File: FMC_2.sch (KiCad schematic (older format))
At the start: 14 parts, among them P2 SAMTEC_ASP-134486-01

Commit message: FMC HPC & LPC done, FPGA power delivery done, RGMII lines done,  MGT lines progress
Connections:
- net labels added: FMC2_DP0_C2M_N, FMC2_DP0_C2M_P, FMC2_DP0_M2C_N, FMC2_DP0_M2C_P
- wire segments 599 -> 603
- no-connect marks 5 -> 1
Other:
- moved on the sheet: C10, C9, P2A, P2B, P2E, P2F, P2I, P2J, R258, R259

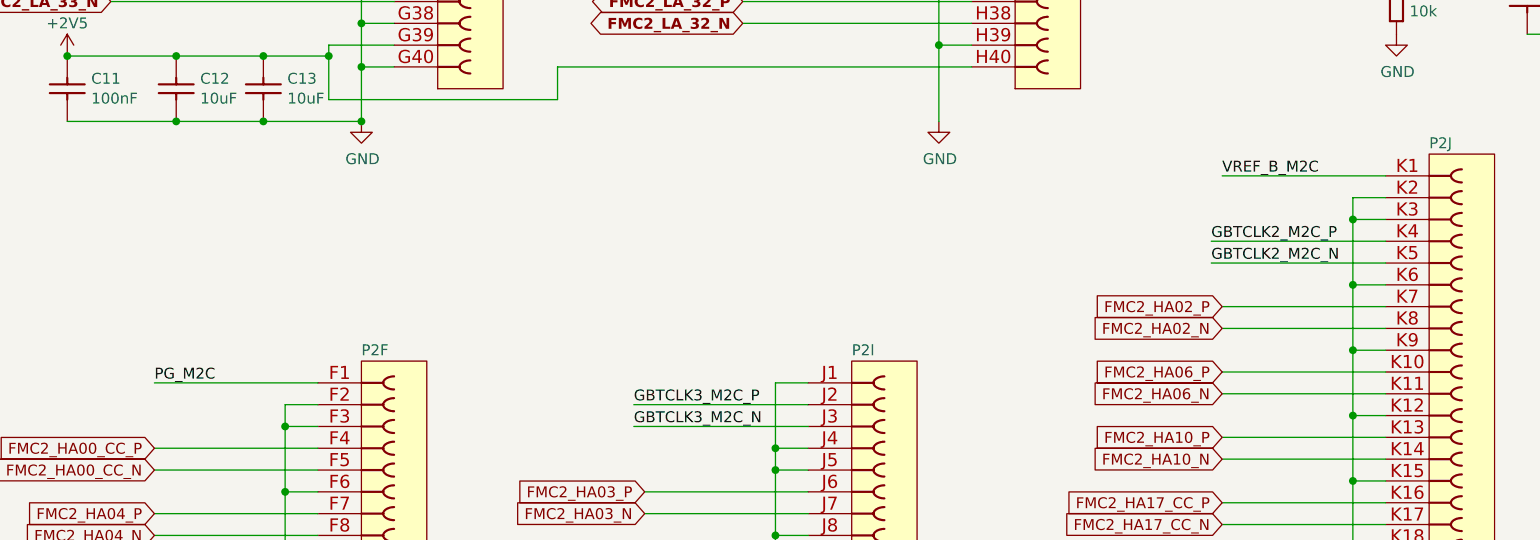
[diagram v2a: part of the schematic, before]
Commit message: FPGA power finished, significant progress on PCB
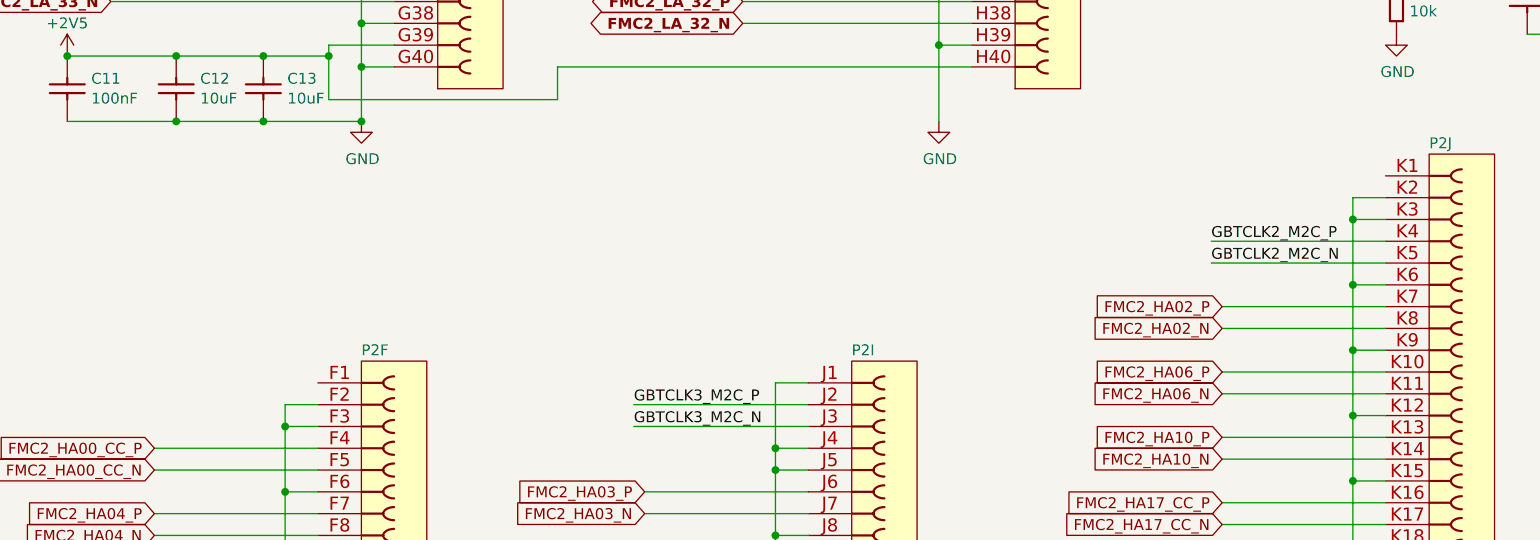
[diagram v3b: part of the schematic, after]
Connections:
- net labels removed: PG_M2C, VREF_B_M2C
- wire segments 603 -> 601
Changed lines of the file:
@@
 	13700 950  14600 950
 $Comp
-L AMC_FMC_Carrier-PcbDoc-rescue:+12V_FMC2-powerMG-AMC_FMC_Carrier-PcbDoc-rescue #PWR01
+L AMC_FMC_Carrier-PcbDoc-rescue:+12V_FMC2-powerMG-AMC_FMC_Carrier-PcbDoc-rescue-AMC_FMC_Carrier-PcbDoc-rescue-AMC_FMC_Carrier-PcbDoc-rescue #PWR01
 U 1 1 5BFC3656
 P 2200 4650
@@
 	6100 6900 6100 7000
 Wire Wire Line
-	7500 6600 8250 6600
-Wire Wire Line
 	7500 6900 8250 6900
 Wire Wire Line
@@
 Wire Wire Line
 	12400 9550 13150 9550
-Wire Wire Line
-	12400 5650 13150 5650
 Text Label 12350 5950 0    50   ~ 0
 GBTCLK2_M2C_P
@@
 Text GLabel 12400 9350 0    50   Input ~ 0
 FMC2_HB17_CC_N
-Text Label 12400 5650 0    50   ~ 0
-VREF_B_M2C
-Text Label 7500 6600 0    50   ~ 0
-PG_M2C
 $Comp
 L power:+2V5 #PWR0678

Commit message: new board outline, rearranging banks connections, SODIMM memory
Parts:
- removed F1: FUS0603_BOURNS-SF-0603F050-2, FUSC1608X55N, symbol Fuses:FUS0603_BOURNS-SF-0603F050-2
- added R78: R0603_10R_1%_0.1W_200PPM, Resistors SMD:RESC1608X55N, symbol Resistors_SMD:R0603_10R_1%_0.1W_200PPM
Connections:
- net labels added: FMC2_GBTCLK1_M2C_N, FMC2_GBTCLK1_M2C_P, PG_M2C, VREF_B_M2C
- net labels removed: GBTCLK1_M2C_N, GBTCLK1_M2C_P
- wire segments 601 -> 605
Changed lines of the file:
@@
 EESchema Schematic File Version 4
-LIBS:AMC_FMC_Carrier-PcbDoc-cache
 EELAYER 30 0
 EELAYER END
@@
 Text Label 13750 1600 0    50   ~ 10
 I2C_FMC2_SDA
-Text Label 13700 3450 0    50   ~ 10
+Text Label 13700 2800 0    50   ~ 10
 FMC2_GBTCLK0_M2C_P
-Text Label 13700 3550 0    50   ~ 10
+Text Label 13700 2900 0    50   ~ 10
 FMC2_GBTCLK0_M2C_N
 Text Label 13750 2250 0    50   ~ 10
@@
 Wire Wire Line
 	13700 4050 14600 4050
-Text HLabel 14600 3450 2    50   Output ~ 10
+Text HLabel 14600 2800 2    50   Output ~ 10
 FMC2_GBTCLK0_M2C_P
-Text HLabel 14600 3550 2    50   Output ~ 10
+Text HLabel 14600 2900 2    50   Output ~ 10
 FMC2_GBTCLK0_M2C_N
 Text HLabel 14600 3700 2    50   Output ~ 10
@@
 FMC2_CLK0_M2C_N
 Wire Wire Line
-	13700 3450 14600 3450
+	13700 2800 14600 2800
 Wire Wire Line
-	13700 3550 14600 3550
+	13700 2900 14600 2900
 Text HLabel 14600 1150 2    50   Output ~ 10
 FMC2_PRSNT_M2C_L
@@
 	13700 950  14600 950
 $Comp
-L AMC_FMC_Carrier-PcbDoc-rescue:+12V_FMC2-powerMG-AMC_FMC_Carrier-PcbDoc-rescue-AMC_FMC_Carrier-PcbDoc-rescue-AMC_FMC_Carrier-PcbDoc-rescue #PWR01
+L AMC_FMC_Carrier-PcbDoc-rescue:+12V_FMC2-powerMG-AMC_FMC_Carrier-PcbDoc-rescue-AMC_FMC_Carrier-PcbDoc-rescue #PWR01
 U 1 1 5BFC3656
 P 2200 4650
@@
 	1    0    0    -1
 $EndComp
-Wire Wire Line
-	15000 4700 15150 4700
 $Comp
 L power:+2V5 #PWR?
@@
 Connection ~ 2200 4650
 Connection ~ 2200 4950
-$Comp
-L Fuses:FUS0603_BOURNS-SF-0603F050-2 F?
-U 1 1 5DA6452C
-P 14700 4700
-AR Path="/5BD31F9A/5DA6452C" Ref="F?"  Part="1"
-AR Path="/5BD31F9F/5DA6452C" Ref="F1"  Part="1"
-F 0 "F1" H 14850 4897 50  0000 C CNN
-F 1 "FUS0603_BOURNS-SF-0603F050-2" H 14700 4480 60  0001 L CNN
-F 2 "FUSC1608X55N" H 14700 3670 60  0001 L CNN
-F 3 "\\\\cern.ch\\dfs\\Applications\\Altium\\Datasheets\\FUSE_BOURNS_SF-0603F.pdf" H 14700 4300 60  0001 L CNN
-F 4 "500mA-50V" H 14850 4806 50  0000 C CNN "~"
-F 5 "FUS0603_BOURNS-SF-0603F050-2" H 14700 4210 60  0001 L CNN "Part Number"
-F 6 "Fuse" H 14700 4120 60  0001 L CNN "Library Ref"
-F 7 "SchLib\\Fuses.SchLib" H 14700 4030 60  0001 L CNN "Library Path"
-F 8 "=Value" H 14700 3940 60  0001 L CNN "Comment"
-F 9 "Standard" H 14700 3850 60  0001 L CNN "Component Kind"
-F 10 "Standard" H 14700 3760 60  0001 L CNN "Component Type"
-F 11 "2" H 14700 3580 60  0001 L CNN "Pin Count"
-F 12 "~~" H 14700 3490 60  0001 L CNN "Case"
-F 13 "PcbLib\\Fuses.PcbLib" H 14700 3400 60  0001 L CNN "Footprint Path"
-F 14 "FUSC1608X55N" H 14700 3310 60  0001 L CNN "Footprint Ref"
-F 15 "Chip Fuse, 2-Leads, Body 1.6mm x 0.8mm, IPC Medium Density" H 14700 3220 60  0001 L CNN "PackageDescription"
-F 16 "Fuse" H 14700 3130 60  0001 L CNN "Family"
-F 17 "Yes" H 14700 3040 60  0001 L CNN "Mounted"
-F 18 "No" H 14700 2950 60  0001 L CNN "Socket"
-F 19 "Yes" H 14700 2860 60  0001 L CNN "SMD"
-F 20 "No" H 14700 2770 60  0001 L CNN "PressFit"
-F 21 "No" H 14700 2680 60  0001 L CNN "Sense"
-F 22 "~~" H 14700 2590 60  0001 L CNN "Sense Comment"
-F 23 "~~" H 14700 2500 60  0001 L CNN "Status"
-F 24 "~~" H 14700 2410 60  0001 L CNN "Status Comment"
-F 25 "~~" H 14700 2320 60  0001 L CNN "SCEM"
-F 26 "500mA-50V" H 14700 2230 60  0001 L CNN "Val"
-F 27 "Thin Film Chip Fuse" H 14700 2140 60  0001 L CNN "Part Description"
-F 28 "BOURNS" H 14700 2050 60  0001 L CNN "Manufacturer"
-F 29 "SF-0603F050-2" H 14700 1960 60  0001 L CNN "Manufacturer Part Number"
-F 30 "0.55mm" H 14700 1870 60  0001 L CNN "ComponentHeight"
-F 31 "~~" H 14700 1780 60  0001 L CNN "Manufacturer1 Example"
-F 32 "~~" H 14700 1690 60  0001 L CNN "Manufacturer1 Part Number"
-F 33 "~~" H 14700 1600 60  0001 L CNN "Manufacturer1 ComponentHeight"
-F 34 "\\\\cern.ch\\dfs\\Applications\\Altium\\Datasheets\\FUSE_BOURNS_SF-0603F.pdf" H 14700 1510 60  0001 L CNN "HelpURL"
-F 35 "~~" H 14700 1420 60  0001 L CNN "ComponentLink1URL"
-F 36 "~~" H 14700 1330 60  0001 L CNN "ComponentLink1Description"
-F 37 "~~" H 14700 1240 60  0001 L CNN "ComponentLink2URL"
-F 38 "~~" H 14700 1150 60  0001 L CNN "ComponentLink2Description"
-F 39 "CERN DEM JLC" H 14700 1060 60  0001 L CNN "Author"
-F 40 "02/01/17 00:00:00" H 14700 970 60  0001 L CNN "CreateDate"
-F 41 "02/01/17 00:00:00" H 14700 880 60  0001 L CNN "LatestRevisionDate"
-F 42 "Fuses" H 14700 790 60  0001 L CNN "Library Name"
-F 43 "This work is licensed under the Creative Commons CC-BY-SA 4.0 License. To the extent that circuit schematics that use Licensed Material can be considered to be ‘Adapted Material’, then the copyright holder waives article 3.b of the license with respect to these schematics." H 14700 700 60  0001 L CNN "License"
-	1    14700 4700
-	1    0    0    -1
-$EndComp
 Text GLabel 10200 1850 0    50   BiDi ~ 10
 FMC2_LA_2_P
@@
 Wire Wire Line
 	3900 8000 3900 8300
-Text Label 3250 8500 0    50   ~ 0
-GBTCLK1_M2C_P
-Text Label 3250 8600 0    50   ~ 0
-GBTCLK1_M2C_N
-Wire Wire Line
-	3250 8500 4050 8500
-Wire Wire Line
-	3250 8600 4050 8600
 Wire Wire Line
 	3900 10300 4050 10300
@@
 	6100 6900 6100 7000
 Wire Wire Line
+	7500 6600 8250 6600
+Wire Wire Line
 	7500 6900 8250 6900
 Wire Wire Line
@@
 Wire Wire Line
 	12400 9550 13150 9550
+Wire Wire Line
+	12400 5650 13150 5650
 Text Label 12350 5950 0    50   ~ 0
 GBTCLK2_M2C_P
@@
 Text GLabel 12400 9350 0    50   Input ~ 0
 FMC2_HB17_CC_N
+Text Label 12400 5650 0    50   ~ 0
+VREF_B_M2C
+Text Label 7500 6600 0    50   ~ 0
+PG_M2C
 $Comp
 L power:+2V5 #PWR0678
@@
 Wire Wire Line
 	2450 1850 3550 1850
+$Comp
+L Resistors_SMD:R0603_10R_1%_0.1W_200PPM R78
+U 1 1 5EBACC52
+P 14700 4700
+F 0 "R78" H 14850 4897 50  0000 C CNN
+F 1 "R0603_10R_1%_0.1W_200PPM" H 14700 4505 50  0001 L CNN
+F 2 "Resistors SMD:RESC1608X55N" H 14700 4430 50  0001 L CNN
+F 3 " " H 14700 4355 50  0001 L CNN
+F 4 "10" H 14850 4806 50  0000 C CNN "Val"
+F 5 "R0603_10R_1%_0.1W_200PPM" H 14700 4280 50  0001 L CNN "Part Number"
+F 6 "Resistor - 1%" H 14700 4205 50  0001 L CNN "Library Ref"
+F 7 "SchLib\\Resistors.SchLib" H 14700 4130 50  0001 L CNN "Library Path"
+F 8 "10" H 14700 4055 50  0001 L CNN "Comment"
+F 9 "Standard" H 14700 3980 50  0001 L CNN "Component Kind"
+F 10 "Standard" H 14700 3905 50  0001 L CNN "Component Type"
+F 11 " " H 14700 3830 50  0001 L CNN "PackageDescription"
+F 12 "2" H 14700 3755 50  0001 L CNN "Pin Count"
+F 13 "PcbLib\\Resistors SMD.PcbLib" H 14700 3680 50  0001 L CNN "Footprint Path"
+F 14 "RESC1608X55N" H 14700 3605 50  0001 L CNN "Footprint Ref"
+F 15 "Preferred" H 14700 3530 50  0001 L CNN "Status"
+F 16 "0.1W" H 14700 3455 50  0001 L CNN "Power"
+F 17 "±200ppm/°C" H 14700 3380 50  0001 L CNN "TC"
+F 18 " " H 14700 3305 50  0001 L CNN "Voltage"
+F 19 "±1%" H 14700 3230 50  0001 L CNN "Tolerance"
+F 20 "General Purpose Thick Film Chip Resistor" H 14700 3155 50  0001 L CNN "Part Description"
+F 21 "GENERIC" H 14700 3080 50  0001 L CNN "Manufacturer"
+F 22 "R0603_10R_1%_0.1W_200PPM" H 14700 3005 50  0001 L CNN "Manufacturer Part Number"
+F 23 "0603" H 14700 2930 50  0001 L CNN "Case"
+F 24 "No" H 14700 2855 50  0001 L CNN "PressFit"
+F 25 "Yes" H 14700 2780 50  0001 L CNN "Mounted"
+F 26 " " H 14700 2705 50  0001 L CNN "Sense Comment"
+F 27 "No" H 14700 2630 50  0001 L CNN "Sense"
+F 28 " " H 14700 2555 50  0001 L CNN "Status Comment"
+F 29 "No" H 14700 2480 50  0001 L CNN "Socket"
+F 30 "Yes" H 14700 2405 50  0001 L CNN "SMD"
+F 31 " " H 14700 2330 50  0001 L CNN "ComponentHeight"
+F 32 "NIC COMPONENT" H 14700 2255 50  0001 L CNN "Manufacturer1 Example"
+F 33 "NRC06F10R0TRF" H 14700 2180 50  0001 L CNN "Manufacturer1 Part Number"
+F 34 "0.55mm" H 14700 2105 50  0001 L CNN "Manufacturer1 ComponentHeight"
+F 35 "CERN DEM JLC" H 14700 2030 50  0001 L CNN "Author"
+F 36 "12/03/07 00:00:00" H 14700 1955 50  0001 L CNN "CreateDate"
+F 37 "06/24/09 00:00:00" H 14700 1880 50  0001 L CNN "LatestRevisionDate"
+F 38 "Resistors SMD" H 14700 1805 50  0001 L CNN "Database Table Name"
+F 39 "Resistors.DbLib" H 14700 1730 50  0001 L CNN "Library Name"
+F 40 "Resistors SMD" H 14700 1655 50  0001 L CNN "Footprint Library"
+F 41 "This work is licensed under the Creative Commons CC-BY-SA 4.0 License. To the extent that circuit schematics that use Licensed Material can be considered to be ‘Adapted Material’, then the copyright holder waives article 3.b of the license with respect to these schematics." H 14700 1580 50  0001 L CNN "License"
+	1    14700 4700
+	1    0    0    -1
+$EndComp
+Wire Wire Line
+	15000 4700 15150 4700
+Text Label 13700 3050 0    50   ~ 10
+FMC2_GBTCLK1_M2C_P
+Text Label 13700 3150 0    50   ~ 10
+FMC2_GBTCLK1_M2C_N
+Text HLabel 14600 3050 2    50   Output ~ 10
+FMC2_GBTCLK1_M2C_P
+Text HLabel 14600 3150 2    50   Output ~ 10
+FMC2_GBTCLK1_M2C_N
+Wire Wire Line
+	13700 3050 14600 3050
+Wire Wire Line
+	13700 3150 14600 3150
+Text Label 2950 8500 0    50   ~ 10
+FMC2_GBTCLK1_M2C_P
+Text Label 2950 8600 0    50   ~ 10
+FMC2_GBTCLK1_M2C_N
+Wire Wire Line
+	2950 8500 4050 8500
+Wire Wire Line
+	2950 8600 4050 8600
 $EndSCHEMATC

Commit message: routing done
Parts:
- removed R78: R0603_10R_1%_0.1W_200PPM, Resistors SMD:RESC1608X55N, symbol Resistors_SMD:R0603_10R_1%_0.1W_200PPM
- added R11, R12: R0402_240R_1%_0.0625W_100PPM, Resistors SMD:RESC1005X40N, symbol Resistors_SMD:R0402_240R_1%_0.0625W_100PPM
- added U55: MIC2090-1YM5TR, ICs And Semiconductors SMD:SOT95P280X145-5N, symbol Analog_&_Interface:MIC2090-1YM5TR
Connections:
- net +3.3VP: now also R258.1, R259.1, U55.1 (VIN)
- net FMC2_3P3VAUX: now also R11.1, U55.5 (VOUT); no longer P2.C34 (c34), R259.1
- net FMC2_FUSE: now also R258.2, U55.4 (FAULT/); no longer R258.1, R259.2
- net GND: now also R12.1, U55.2 (GND); no longer P2.D35 (d35), R258.2
- new net: R259.2, U55.3 (EN)
- new net: P2.C34 (c34), R11.2
- new net: P2.D35 (d35), R12.2
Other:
- moved on the sheet: C10, C5, C6, C9, R258, R259

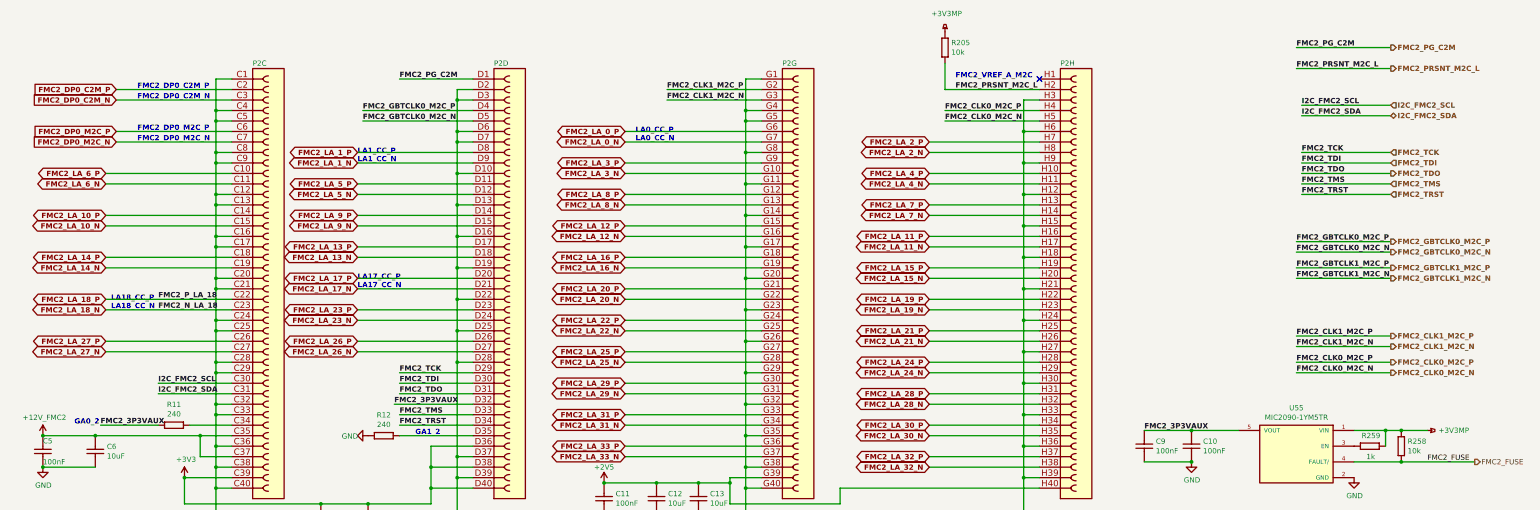
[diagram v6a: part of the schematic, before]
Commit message: DDR lenght mached, 2 additional LEDs added, I2C pullups voltage changed and other minor changes
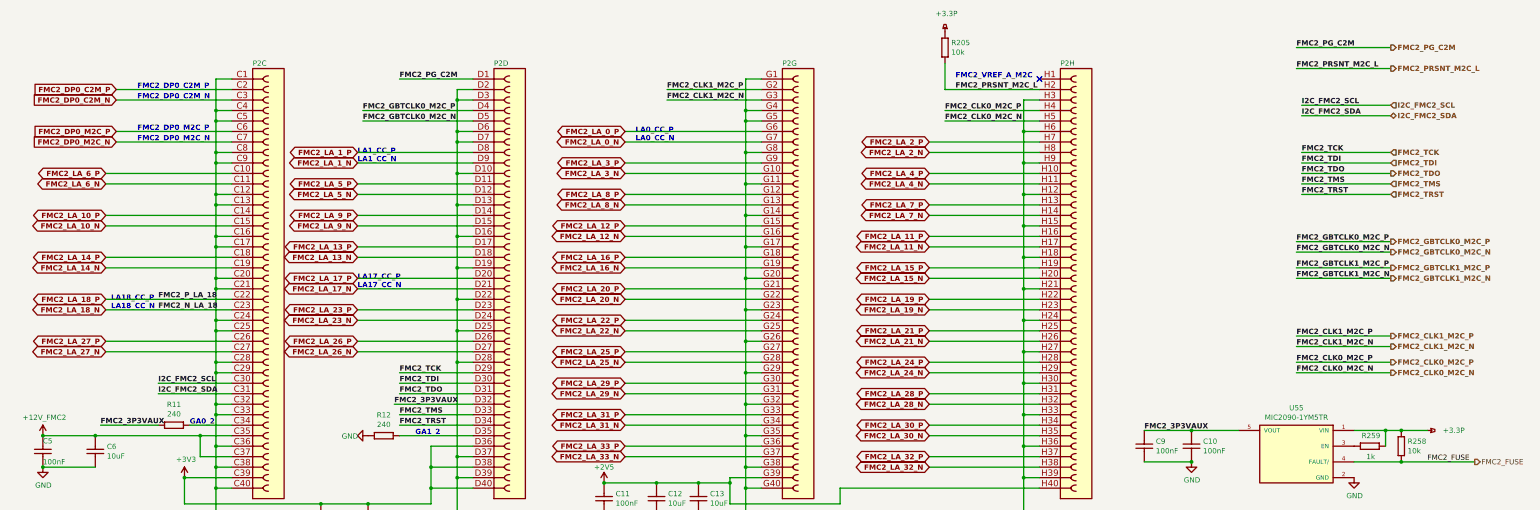
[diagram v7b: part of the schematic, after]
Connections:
- net +3.3VP renamed +3.3P
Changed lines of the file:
@@
 	10350 1350 10350 1100
 $Comp
-L power:+3.3VP #PWR?
+L power2:+3.3P #PWR?
 U 1 1 5EA24411
 P 10350 800
@@
 AR Path="/5EA24411" Ref="#PWR0167"  Part="1"
 F 0 "#PWR0167" H 10350 650 50  0001 C CNN
-F 1 "+3V3MP" H 10365 973 50  0000 C CNN
+F 1 "+3.3P" H 10365 973 50  0000 C CNN
 F 2 "" H 10350 800 50  0001 C CNN
 F 3 "" H 10350 800 50  0001 C CNN
@@
 	10200 4650 11250 4650
 $Comp
-L power:+3.3VP #PWR?
+L power2:+3.3P #PWR?
 U 1 1 5DDA87F3
 P 14950 4600
@@
 AR Path="/5DDA87F3" Ref="#PWR0549"  Part="1"
 F 0 "#PWR0549" H 14950 4450 50  0001 C CNN
-F 1 "+3V3MP" V 14950 4850 50  0000 C CNN
+F 1 "+3.3P" V 14950 4850 50  0000 C CNN
 F 2 "" H 14950 4600 50  0001 C CNN
 F 3 "" H 14950 4600 50  0001 C CNN
@@
 Text Label 2300 4550 0    50   ~ 10
 FMC2_3P3VAUX
-Text Notes 2050 4550 0    50   ~ 10
+Text Notes 3150 4550 0    50   ~ 10
 GA0_2
 $Comp
